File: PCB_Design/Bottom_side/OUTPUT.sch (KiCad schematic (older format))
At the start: 4 parts, among them Q1 Q_NMOS_GSD, Q2 Q_NMOS_GSD, Q3 Q_NMOS_GSD, Q4 Q_NMOS_GSD

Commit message: PCB bottom layer populated
PCB bottom layer populated, and waiting for top layer to be merged.
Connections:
- net BATT_V_OUT_2: now also Q2.2 (S)
- net Sheet5A5E5DCD/I_out renamed Ina_BV_1/I_out
- net Sheet5A5E5DCD/I_out renamed INA_BV_2/I_out
- net Sheet5A5E5DCD/I_out renamed Ina_5V_Out/I_out
- net Sheet5A5E5DCD/I_out renamed Ina_3V6_Out/I_out
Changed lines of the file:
@@
 LIBS:contrib
 LIBS:valves
-LIBS:Custom_Library
 LIBS:Bottom_side-cache
 EELAYER 25 0
@@
 $Descr A4 11693 8268
 encoding utf-8
-Sheet 17 25
+Sheet 17 26
 Title ""
 Date ""
@@
 S 1600 1150 1650 850
 U 5A5E496B
-F0 "5VBuck" 60
+F0 "5VBuck1" 60
 F1 "5VBuck.sch" 60
 F2 "ENABLE_5V" I L 1600 1700 60
@@
 S 1600 2400 1650 850
 U 5A5E5DCC
-F0 "5VBuck" 60
+F0 "5VBuck2" 60
 F1 "5VBuck.sch" 60
 F2 "ENABLE_5V" I L 1600 3000 60
@@
 S 3650 1150 700  500
 U 5A5E5DCE
-F0 "Sheet5A5E5DCD" 60
+F0 "Ina_5V_Out" 60
 F1 "INA_5V_OUT.sch" 60
 F2 "3V3" I R 4350 1300 60
@@
 S 3650 1900 700  500
 U 5A5E7852
-F0 "Sheet5A5E5DCD" 60
+F0 "Ina_3V6_Out" 60
 F1 "INA_5V_OUT.sch" 60
 F2 "3V3" I R 4350 2050 60
@@
 S 1600 3700 700  500
 U 5A5E7CAE
-F0 "Sheet5A5E5DCD" 60
+F0 "Ina_BV_1" 60
 F1 "INA_5V_OUT.sch" 60
 F2 "3V3" I R 2300 3850 60
@@
 S 1600 4450 700  500
 U 5A5E7CB4
-F0 "Sheet5A5E5DCD" 60
+F0 "INA_BV_2" 60
 F1 "INA_5V_OUT.sch" 60
 F2 "3V3" I R 2300 4600 60
@@
 $EndComp
 Wire Wire Line
-	3250 4750 3450 4750
+	3250 4750 3500 4750
 Text HLabel 3150 5050 2    60   Input ~ 0
 CTRL_BATT_V_OUT_2

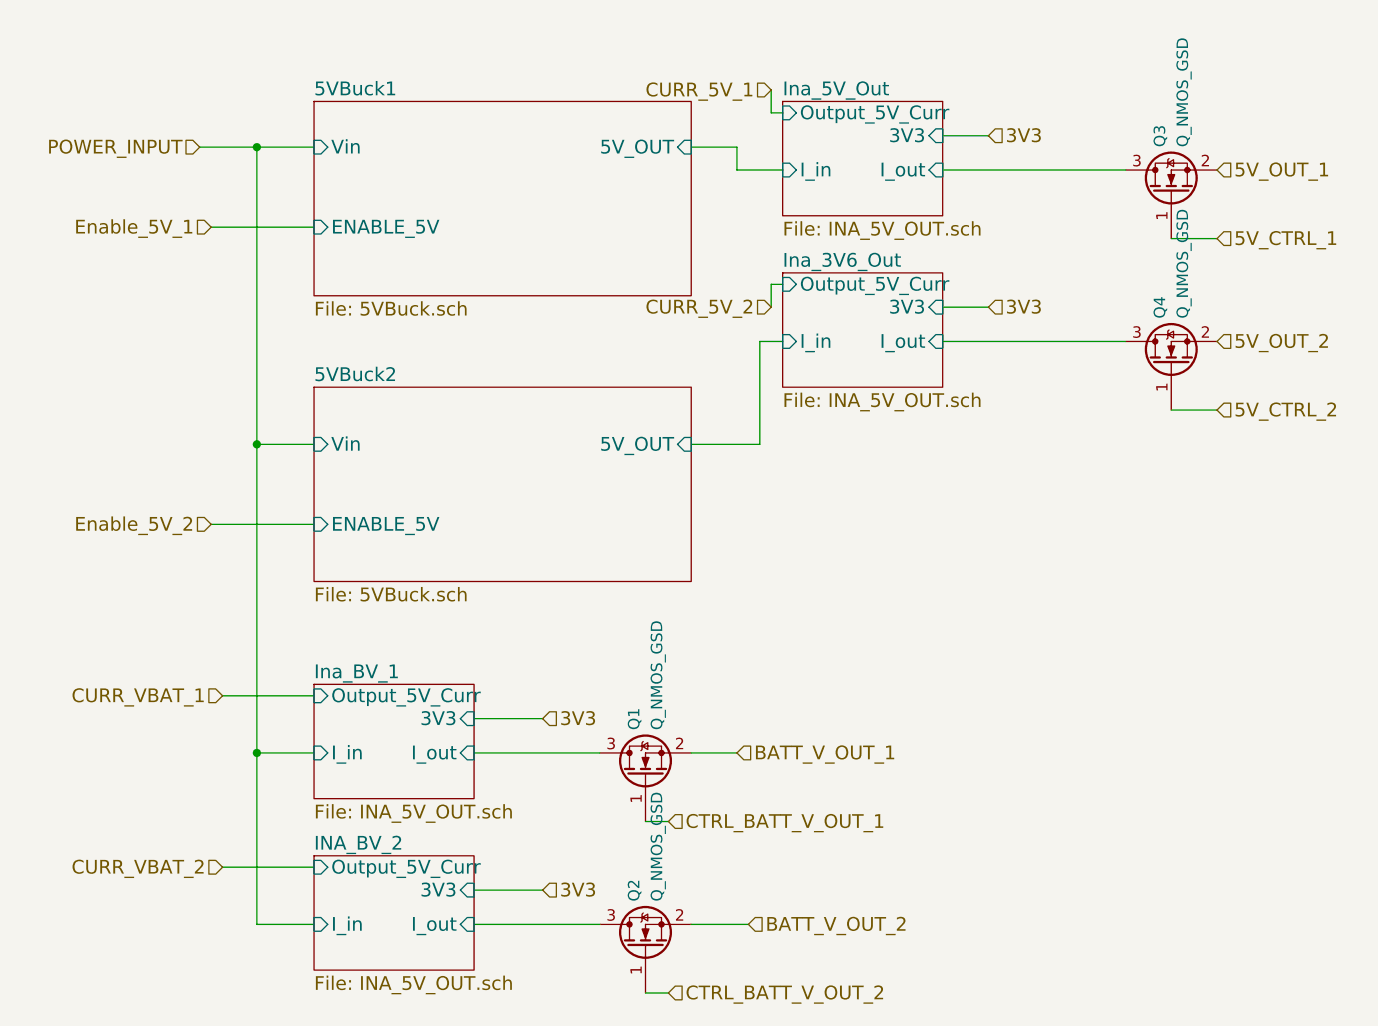
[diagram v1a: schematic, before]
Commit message: Updated PCB structure tree
Full_PCB now includes bottom and top layer hierarchical sheets
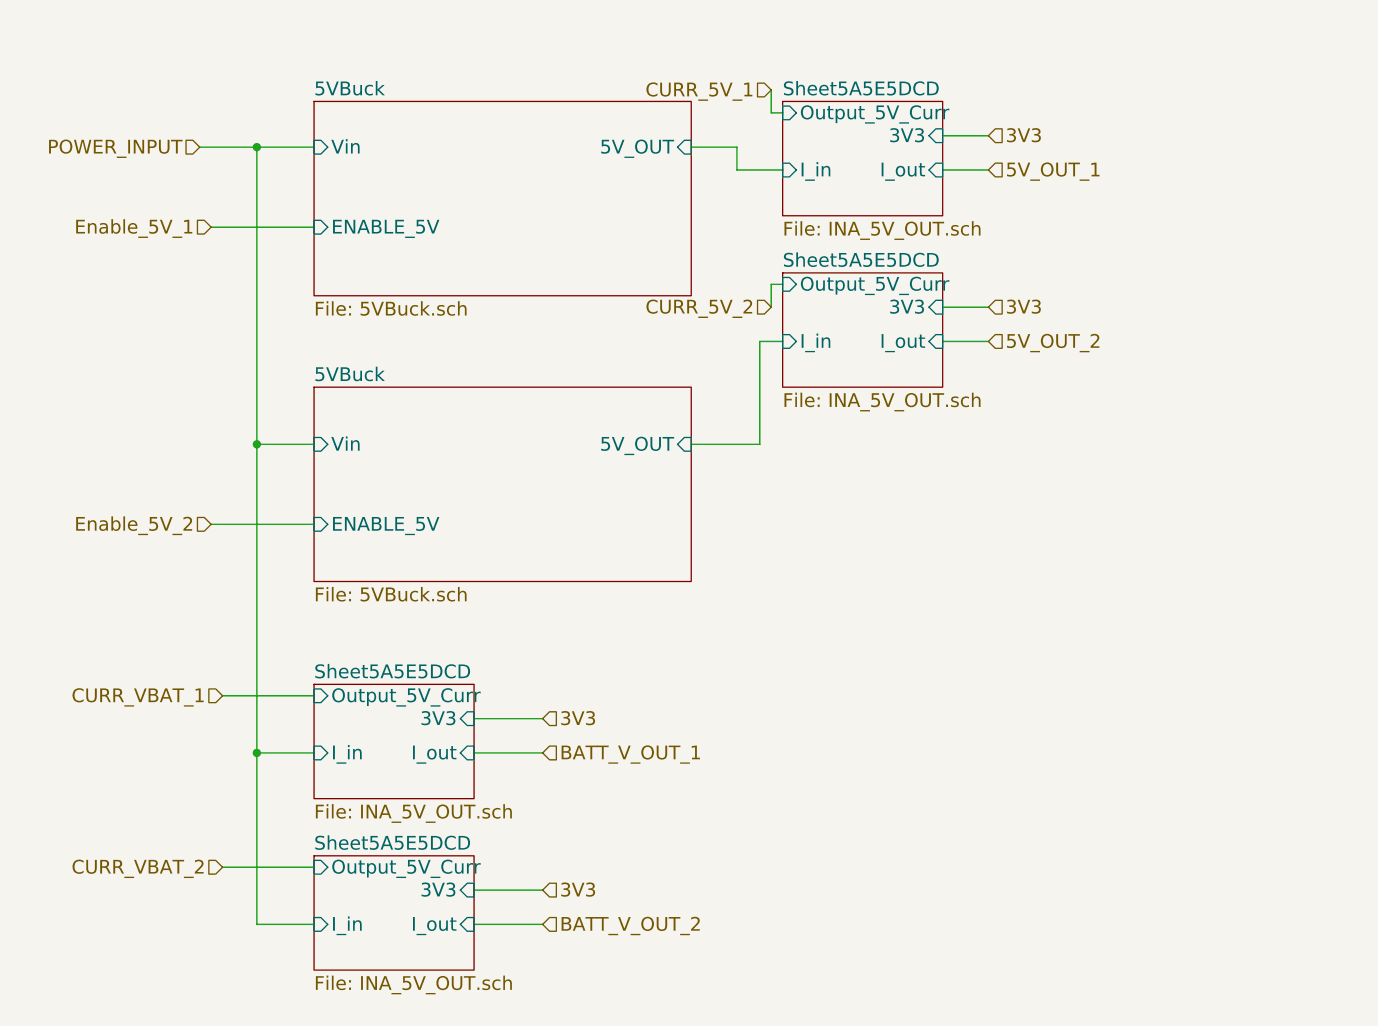
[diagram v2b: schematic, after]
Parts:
- removed Q1, Q2, Q3, Q4: Q_NMOS_GSD, TO_SOT_Packages_SMD:SOT-23, symbol Q_NMOS_GSD
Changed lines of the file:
@@
 LIBS:power
 LIBS:device
-LIBS:switches
-LIBS:relays
-LIBS:motors
 LIBS:transistors
 LIBS:conn
@@
 LIBS:contrib
 LIBS:valves
-LIBS:Bottom_side-cache
+LIBS:Full_PCB-cache
 EELAYER 25 0
 EELAYER END
@@
 S 1600 1150 1650 850
 U 5A5E496B
-F0 "5VBuck1" 60
+F0 "5VBuck" 60
 F1 "5VBuck.sch" 60
 F2 "ENABLE_5V" I L 1600 1700 60
@@
 S 1600 2400 1650 850
 U 5A5E5DCC
-F0 "5VBuck2" 60
+F0 "5VBuck" 60
 F1 "5VBuck.sch" 60
 F2 "ENABLE_5V" I L 1600 3000 60
@@
 S 3650 1150 700  500
 U 5A5E5DCE
-F0 "Ina_5V_Out" 60
+F0 "Sheet5A5E5DCD" 60
 F1 "INA_5V_OUT.sch" 60
 F2 "3V3" I R 4350 1300 60
@@
 Wire Wire Line
 	4550 2050 4350 2050
-Text HLabel 5550 1450 2    60   Input ~ 0
+Text HLabel 4550 1450 2    60   Input ~ 0
 5V_OUT_1
 Wire Wire Line
-	4350 1450 5150 1450
-Text HLabel 5550 2200 2    60   Input ~ 0
+	4350 1450 4550 1450
+Text HLabel 4550 2200 2    60   Input ~ 0
 5V_OUT_2
 Wire Wire Line
-	4350 2200 5150 2200
-Text HLabel 3450 4000 2    60   Input ~ 0
+	4350 2200 4550 2200
+Text HLabel 2600 4000 2    60   Input ~ 0
 BATT_V_OUT_1
 Wire Wire Line
-	2300 4000 2850 4000
+	2300 4000 2600 4000
 $Sheet
 S 3650 1900 700  500
 U 5A5E7852
-F0 "Ina_3V6_Out" 60
+F0 "Sheet5A5E5DCD" 60
 F1 "INA_5V_OUT.sch" 60
 F2 "3V3" I R 4350 2050 60
@@
 S 1600 3700 700  500
 U 5A5E7CAE
-F0 "Ina_BV_1" 60
+F0 "Sheet5A5E5DCD" 60
 F1 "INA_5V_OUT.sch" 60
 F2 "3V3" I R 2300 3850 60
@@
 S 1600 4450 700  500
 U 5A5E7CB4
-F0 "INA_BV_2" 60
+F0 "Sheet5A5E5DCD" 60
 F1 "INA_5V_OUT.sch" 60
 F2 "3V3" I R 2300 4600 60
@@
 Wire Wire Line
 	2300 4600 2600 4600
-Text HLabel 3500 4750 2    60   Input ~ 0
+Text HLabel 2600 4750 2    60   Input ~ 0
 BATT_V_OUT_2
+Wire Wire Line
+	2600 4750 2300 4750
 Wire Wire Line
 	1600 4500 1200 4500
@@
 Text HLabel 1150 3000 0    60   Input ~ 0
 Enable_5V_2
-$Comp
-L Q_NMOS_GSD Q1
-U 1 1 5A68DE04
-P 3050 4100
-F 0 "Q1" H 3250 4150 50  0000 L CNN
-F 1 "Q_NMOS_GSD" H 3250 4050 50  0000 L CNN
-F 2 "TO_SOT_Packages_SMD:SOT-23" H 3250 4200 50  0001 C CNN
-F 3 "" H 3050 4100 50  0001 C CNN
-	1    3050 4100
-	0    -1   -1   0
-$EndComp
-Wire Wire Line
-	3250 4000 3450 4000
-Text HLabel 3150 4300 2    60   Input ~ 0
-CTRL_BATT_V_OUT_1
-Wire Wire Line
-	3150 4300 3050 4300
-Wire Wire Line
-	2300 4750 2850 4750
-$Comp
-L Q_NMOS_GSD Q2
-U 1 1 5A68E2E6
-P 3050 4850
-F 0 "Q2" H 3250 4900 50  0000 L CNN
-F 1 "Q_NMOS_GSD" H 3250 4800 50  0000 L CNN
-F 2 "TO_SOT_Packages_SMD:SOT-23" H 3250 4950 50  0001 C CNN
-F 3 "" H 3050 4850 50  0001 C CNN
-	1    3050 4850
-	0    -1   -1   0
-$EndComp
-Wire Wire Line
-	3250 4750 3500 4750
-Text HLabel 3150 5050 2    60   Input ~ 0
-CTRL_BATT_V_OUT_2
-Wire Wire Line
-	3150 5050 3050 5050
-$Comp
-L Q_NMOS_GSD Q3
-U 1 1 5A68E5D6
-P 5350 1550
-F 0 "Q3" H 5550 1600 50  0000 L CNN
-F 1 "Q_NMOS_GSD" H 5550 1500 50  0000 L CNN
-F 2 "TO_SOT_Packages_SMD:SOT-23" H 5550 1650 50  0001 C CNN
-F 3 "" H 5350 1550 50  0001 C CNN
-	1    5350 1550
-	0    -1   -1   0
-$EndComp
-$Comp
-L Q_NMOS_GSD Q4
-U 1 1 5A68E880
-P 5350 2300
-F 0 "Q4" H 5550 2350 50  0000 L CNN
-F 1 "Q_NMOS_GSD" H 5550 2250 50  0000 L CNN
-F 2 "TO_SOT_Packages_SMD:SOT-23" H 5550 2400 50  0001 C CNN
-F 3 "" H 5350 2300 50  0001 C CNN
-	1    5350 2300
-	0    -1   -1   0
-$EndComp
-Text HLabel 5550 1750 2    60   Input ~ 0
-5V_CTRL_1
-Wire Wire Line
-	5550 1750 5350 1750
-Text HLabel 5550 2500 2    60   Input ~ 0
-5V_CTRL_2
-Wire Wire Line
-	5550 2500 5350 2500
 $EndSCHEMATC
